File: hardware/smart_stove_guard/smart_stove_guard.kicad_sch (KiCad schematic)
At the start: 29 parts, among them IC1 BS412, J1 12401948E412A, J2 AX-1203D-LF, J3 IO Expansion, U1 ESP32-C6-WROOM-1-N4, U2 MLX90614ESF-AAA-000-TU, U3 AMS1117-3.3

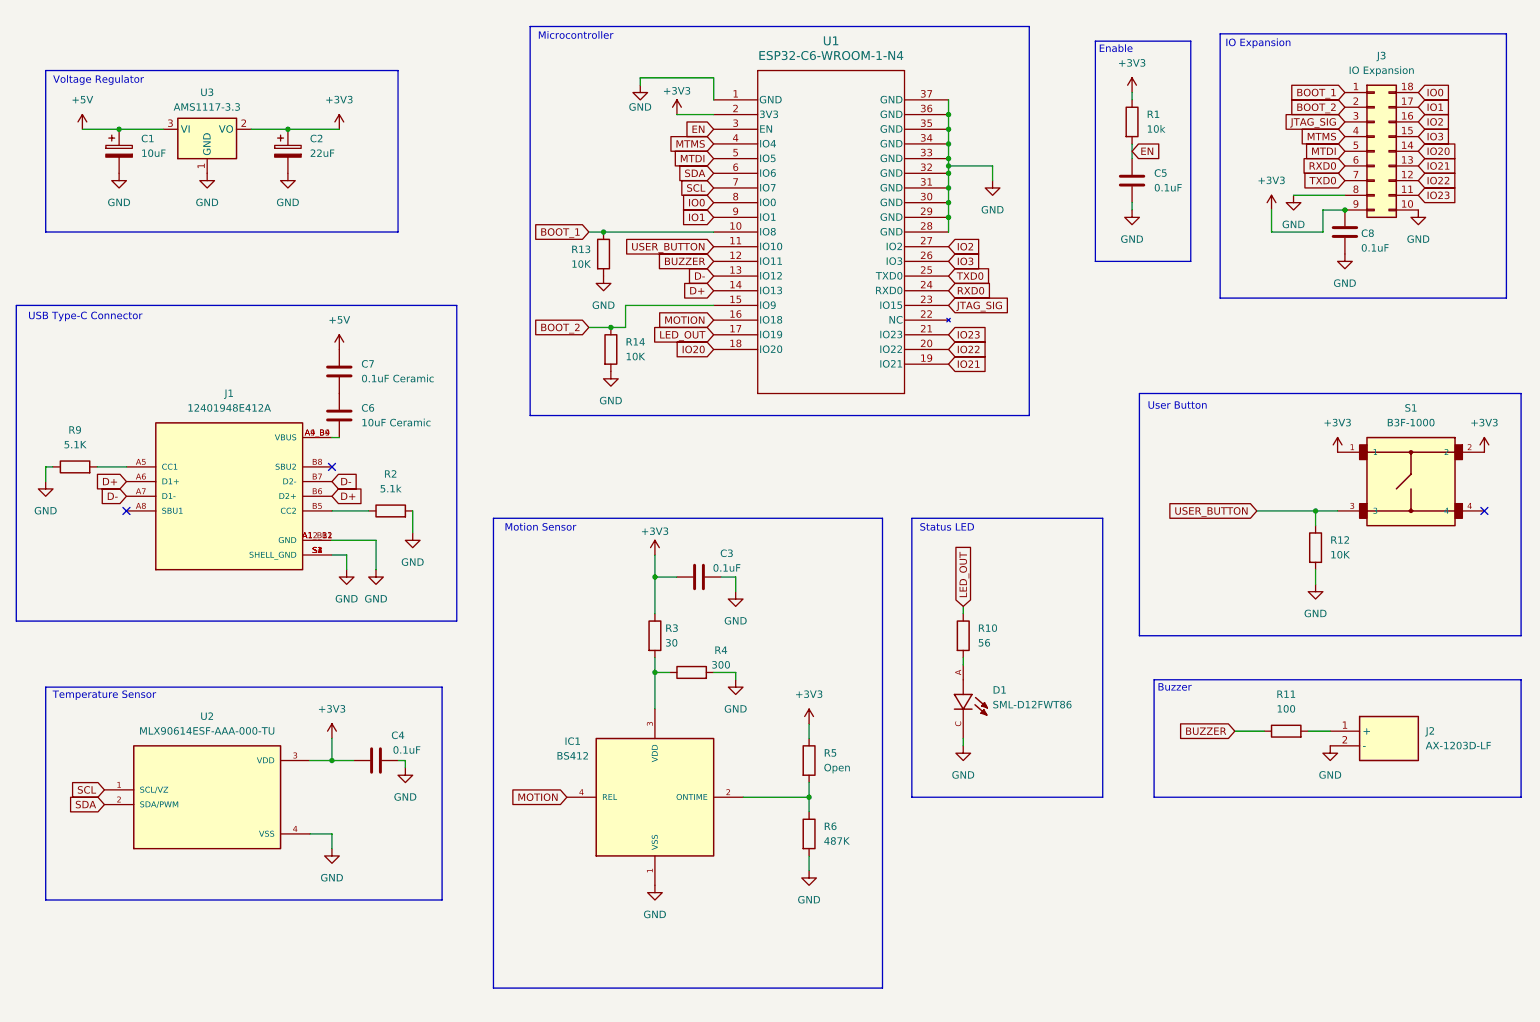
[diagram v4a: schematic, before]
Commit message: Signal Lines + Basic Layout
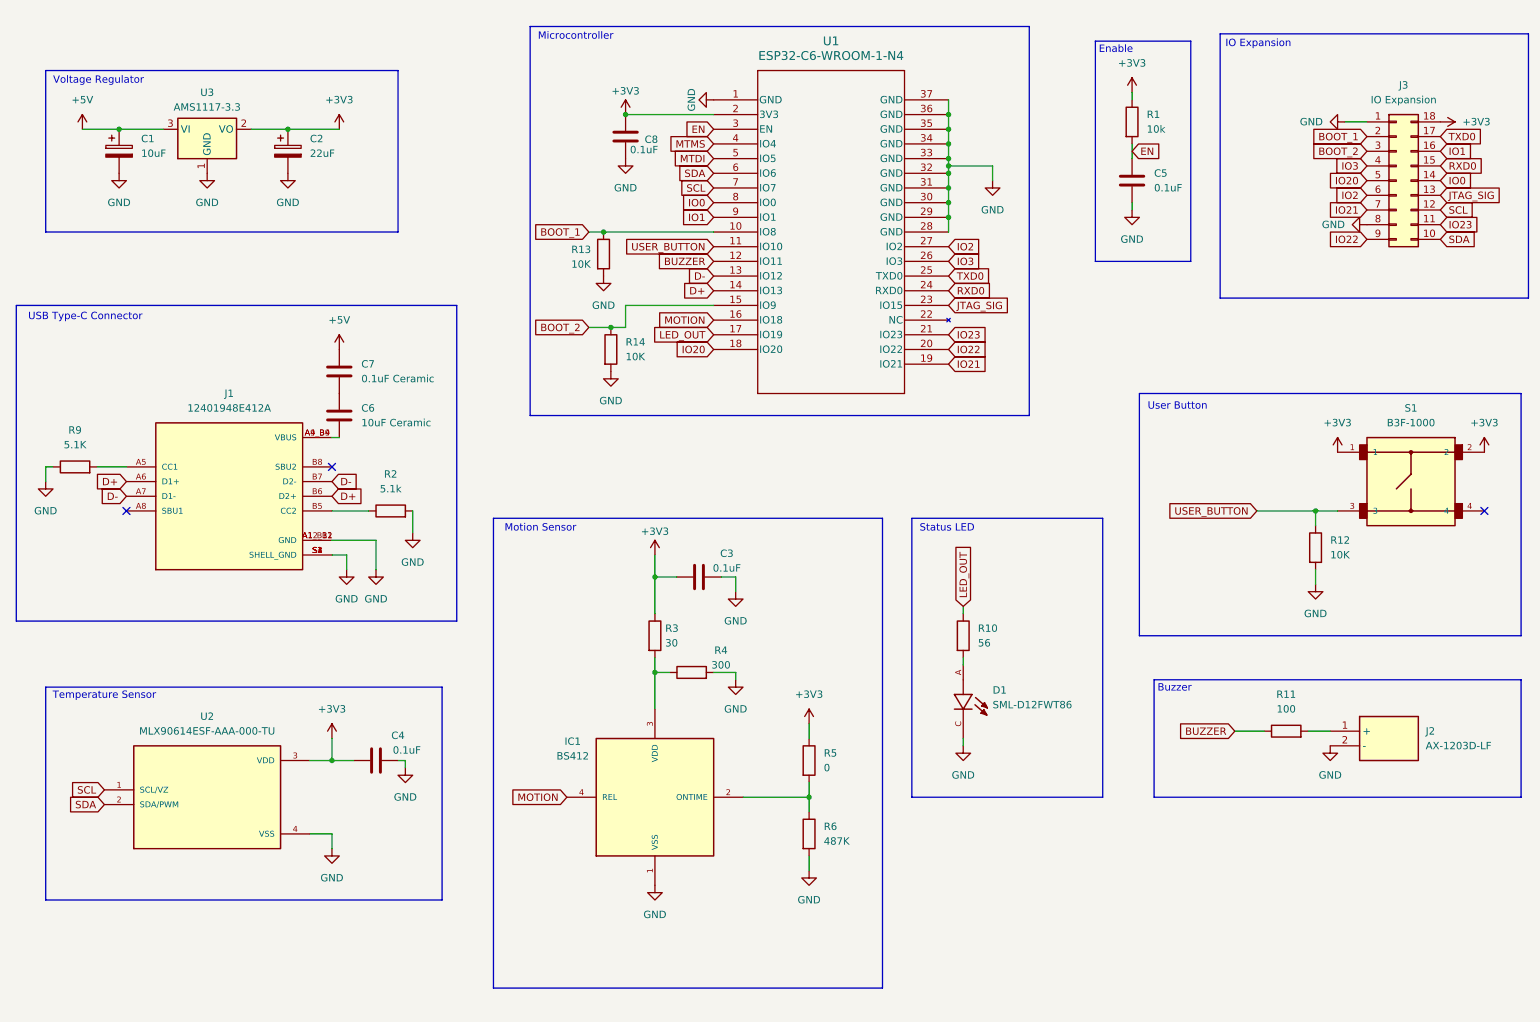
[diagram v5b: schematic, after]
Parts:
- IC1: footprint footprints:BS412 -> smart_stove footprints:BS412
- J1: footprint footprints:AMPHENOL_12401948E412A -> smart_stove footprints:AMPHENOL_12401948E412A
- J2: footprint footprints:AX1203DLF -> smart_stove footprints:AX1203DLF
- R5: value Open -> 0
- S1: footprint footprints:SW_B3F-1000 -> smart_stove footprints:SW_B3F-1000
- U1: footprint footprints:MOD28_ESP32-C6-WROOM-1_EXP -> smart_stove footprints:MOD28_ESP32-C6-WROOM-1_EXP
- U2: footprint footprints:MLX90614ESF-AAA-000 -> smart_stove footprints:MLX90614ESF-AAA-000
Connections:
- net +3V3: now also J3.18 (Pin_18); no longer J3.9 (Pin_9)
- net BOOT_1: now also J3.2 (Pin_2); no longer J3.1 (Pin_1)
- net BOOT_2: now also J3.3 (Pin_3); no longer J3.2 (Pin_2)
- net GND: now also J3.1 (Pin_1); no longer J3.10 (Pin_10)
- net IO0: now also J3.14 (Pin_14); no longer J3.18 (Pin_18)
- net IO1: now also J3.16 (Pin_16); no longer J3.17 (Pin_17)
- net IO2: now also J3.6 (Pin_6); no longer J3.16 (Pin_16)
- net IO20: now also J3.5 (Pin_5); no longer J3.14 (Pin_14)
- net IO21: now also J3.7 (Pin_7); no longer J3.13 (Pin_13)
- net IO22: now also J3.9 (Pin_9); no longer J3.12 (Pin_12)
- net IO3: now also J3.4 (Pin_4); no longer J3.15 (Pin_15)
- net JTAG_SIG: now also J3.13 (Pin_13); no longer J3.3 (Pin_3)
- net MTDI: no longer J3.5 (Pin_5)
- net MTMS: no longer J3.4 (Pin_4)
- net RXD0: now also J3.15 (Pin_15); no longer J3.6 (Pin_6)
- net SCL: now also J3.12 (Pin_12)
- net SDA: now also J3.10 (Pin_10)
- net TXD0: now also J3.17 (Pin_17); no longer J3.7 (Pin_7)
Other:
- moved on the sheet: C8, J3

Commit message: minor changes before continuing layout tonight
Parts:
- added R7, R8: 4.7k, Resistor_SMD:R_0805_2012Metric, symbol Device:R
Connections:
- net +3V3: now also R7.1, R8.1
- net SCL: now also R8.2
- net SDA: now also R7.2
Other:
- moved on the sheet: C8

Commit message: ground pours and mounting
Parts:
- C1, C2: footprint Capacitor_Tantalum_SMD:CP_EIA-7343-31_Kemet-D_HandSolder -> Capacitor_Tantalum_SMD:CP_EIA-3216-10_Kemet-I_HandSolder
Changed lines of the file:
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@@
 	(wire
 		(pts
-			(xy 74.93 116.84) (xy 77.47 116.84)
-		)
-		(stroke
-			(width 0)
-			(type default)
-		)
-	)
-	(wire
-		(pts
 			(xy 119.38 77.47) (xy 123.19 77.47)
 		)
@@
 	(wire
 		(pts
+			(xy 74.93 116.84) (xy 77.47 116.84)
+		)
+		(stroke
+			(width 0)
+			(type default)
+		)
+	)
+	(wire
+		(pts
 			(xy 132.08 29.21) (xy 127 29.21)
 		)
@@
 			)
 		)
-		(property "Footprint" "Capacitor_Tantalum_SMD:CP_EIA-7343-31_Kemet-D_HandSolder"
+		(property "Footprint" "Capacitor_Tantalum_SMD:CP_EIA-3216-10_Kemet-I_HandSolder"
 			(at 39.0652 50.8 0)
 			(effects
@@
 			)
 		)
-		(property "Footprint" "Capacitor_Tantalum_SMD:CP_EIA-7343-31_Kemet-D_HandSolder"
+		(property "Footprint" "Capacitor_Tantalum_SMD:CP_EIA-3216-10_Kemet-I_HandSolder"
 			(at 68.2752 50.8 0)
 			(effects
